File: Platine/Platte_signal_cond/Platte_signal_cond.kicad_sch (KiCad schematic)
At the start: 16 parts

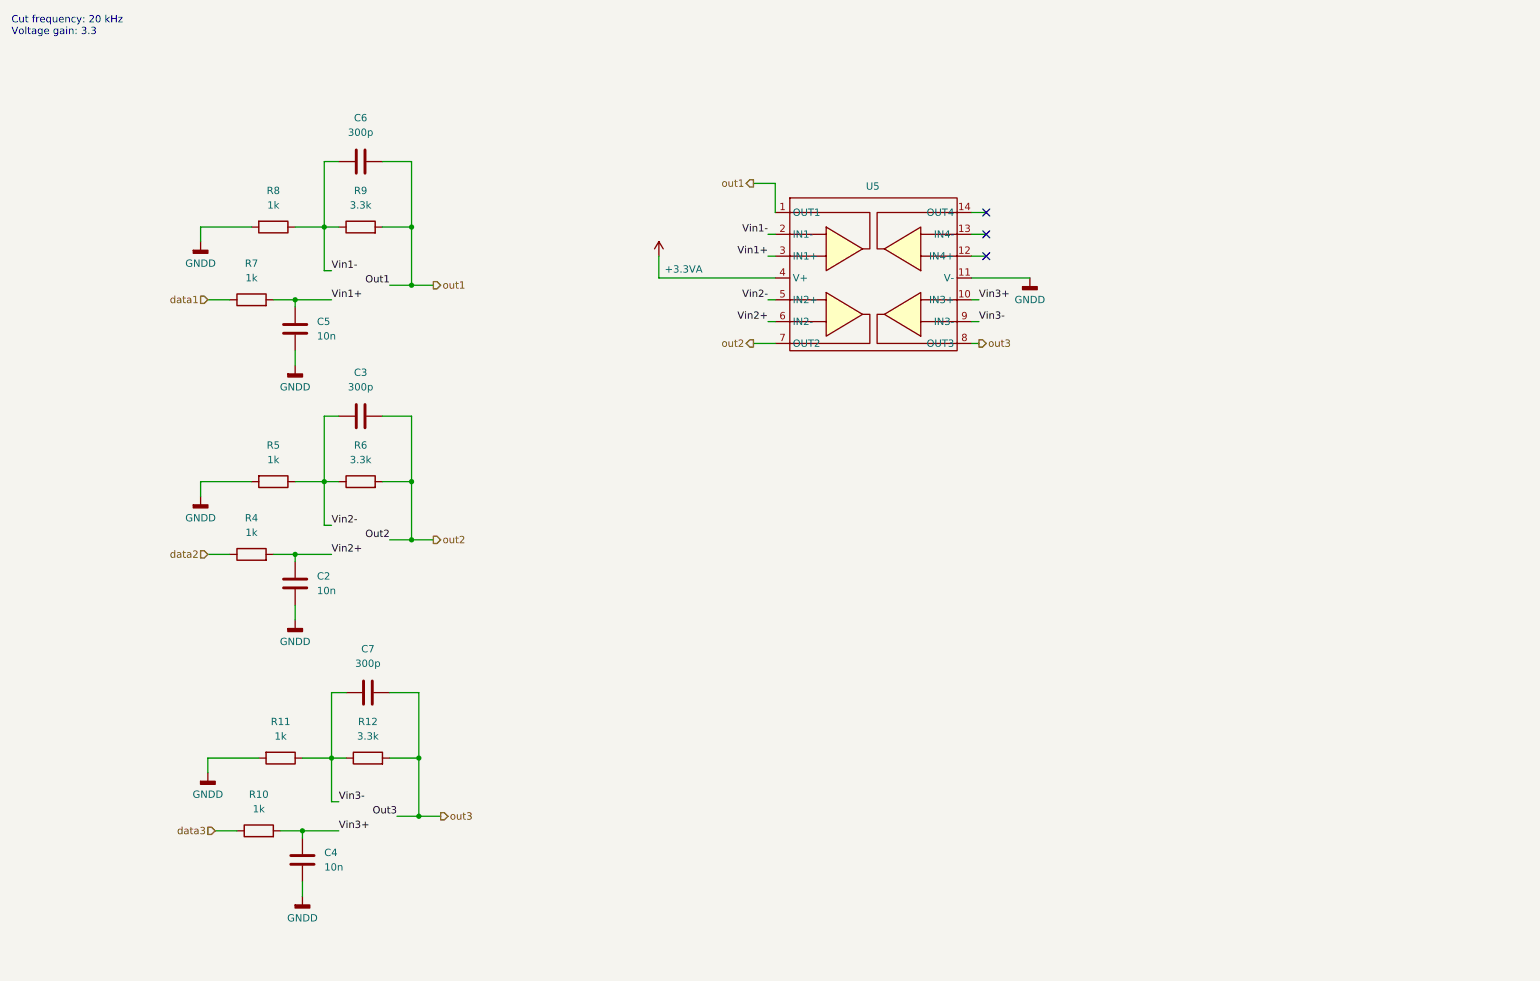
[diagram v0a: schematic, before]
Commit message: Removing CST simulations because of weight, theyre now in the folder outside the repo
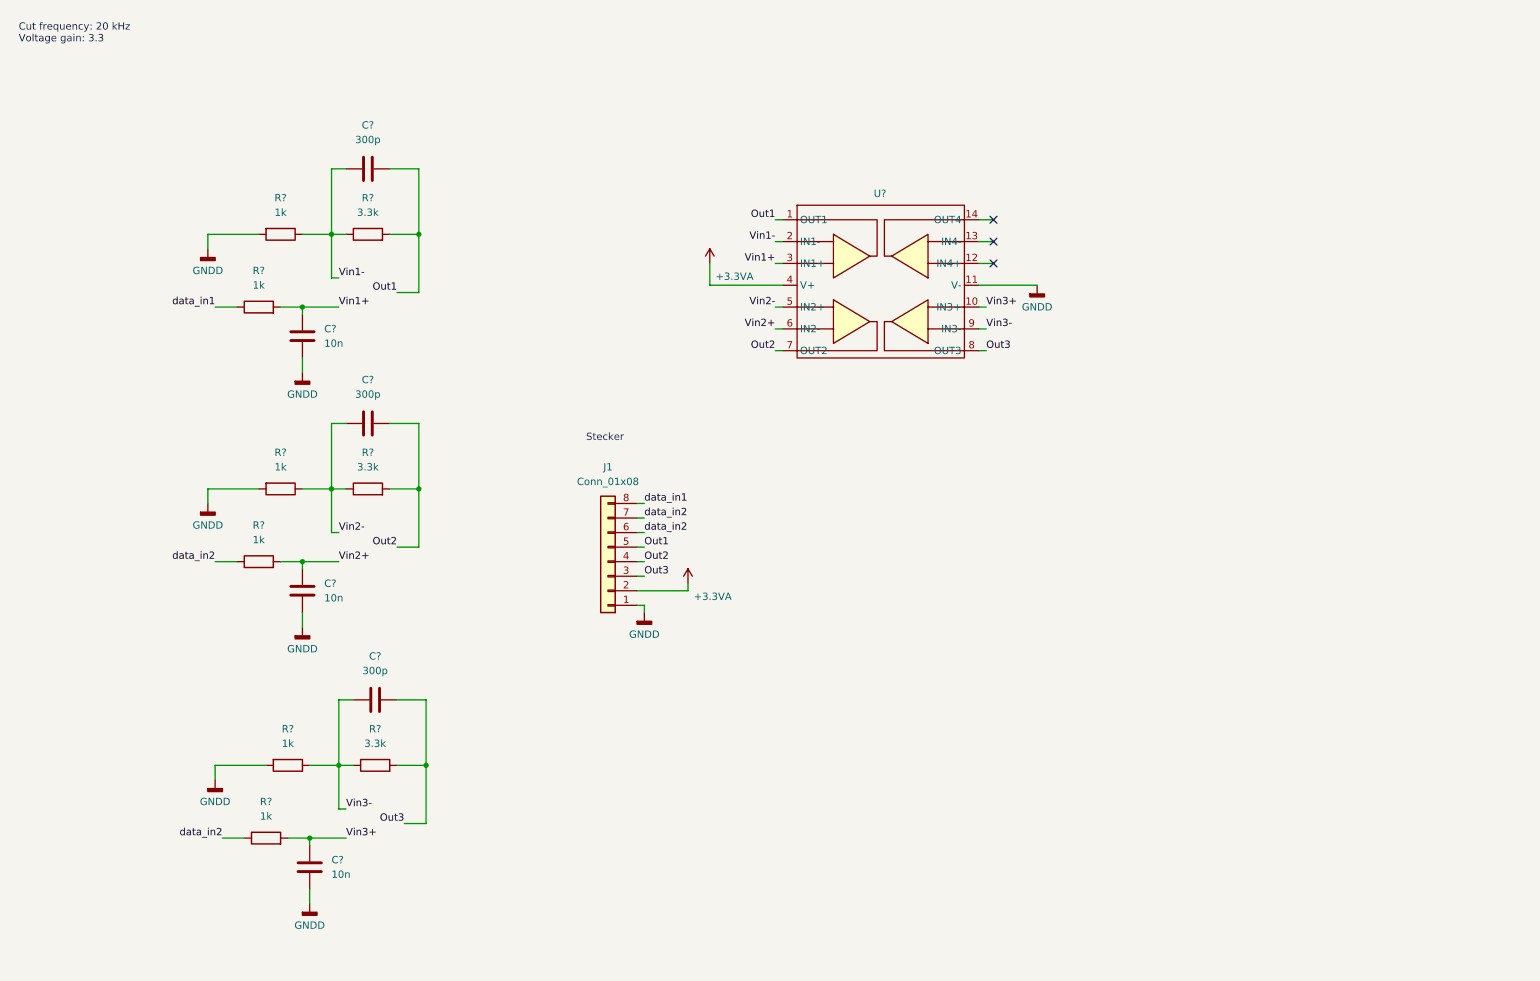
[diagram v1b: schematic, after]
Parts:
- added J1: Conn_01x08, symbol Connector_Generic:Conn_01x08
- U?: renamed from U5; footprint Package_SO:SOIC-14_3.9x8.7mm_P1.27mm -> (none)
- renumbered C4 to C?, C5 to C?, C7 to C?, C3 to C?, C2 to C?, C6 to C?, R4 to R?, R10 to R?, R7 to R?, R11 to R?, R6 to R?, R8 to R?, R12 to R?, R9 to R?, R5 to R?
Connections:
- net data3 is gone; now on net data_in2: R?.1
- net +3.3VA: now also J1.2 (Pin_2)
- net GNDD: now also J1.1 (Pin_1)
- net data1 renamed data_in1
- net data_in1: now also J1.8 (Pin_8)
- net data2 renamed data_in2
- net data_in2: now also J1.6 (Pin_6), J1.7 (Pin_7)
- net out1 renamed Out1
- net Out1: now also J1.5 (Pin_5)
- net out2 renamed Out2
- net Out2: now also J1.4 (Pin_4)
- net out3 renamed Out3
- net Out3: now also J1.3 (Pin_3)
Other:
- note added: "Stecker"
- moved on the sheet: C?, R?, U?

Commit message: Adding footprints to signal conditioning PCB and placing components
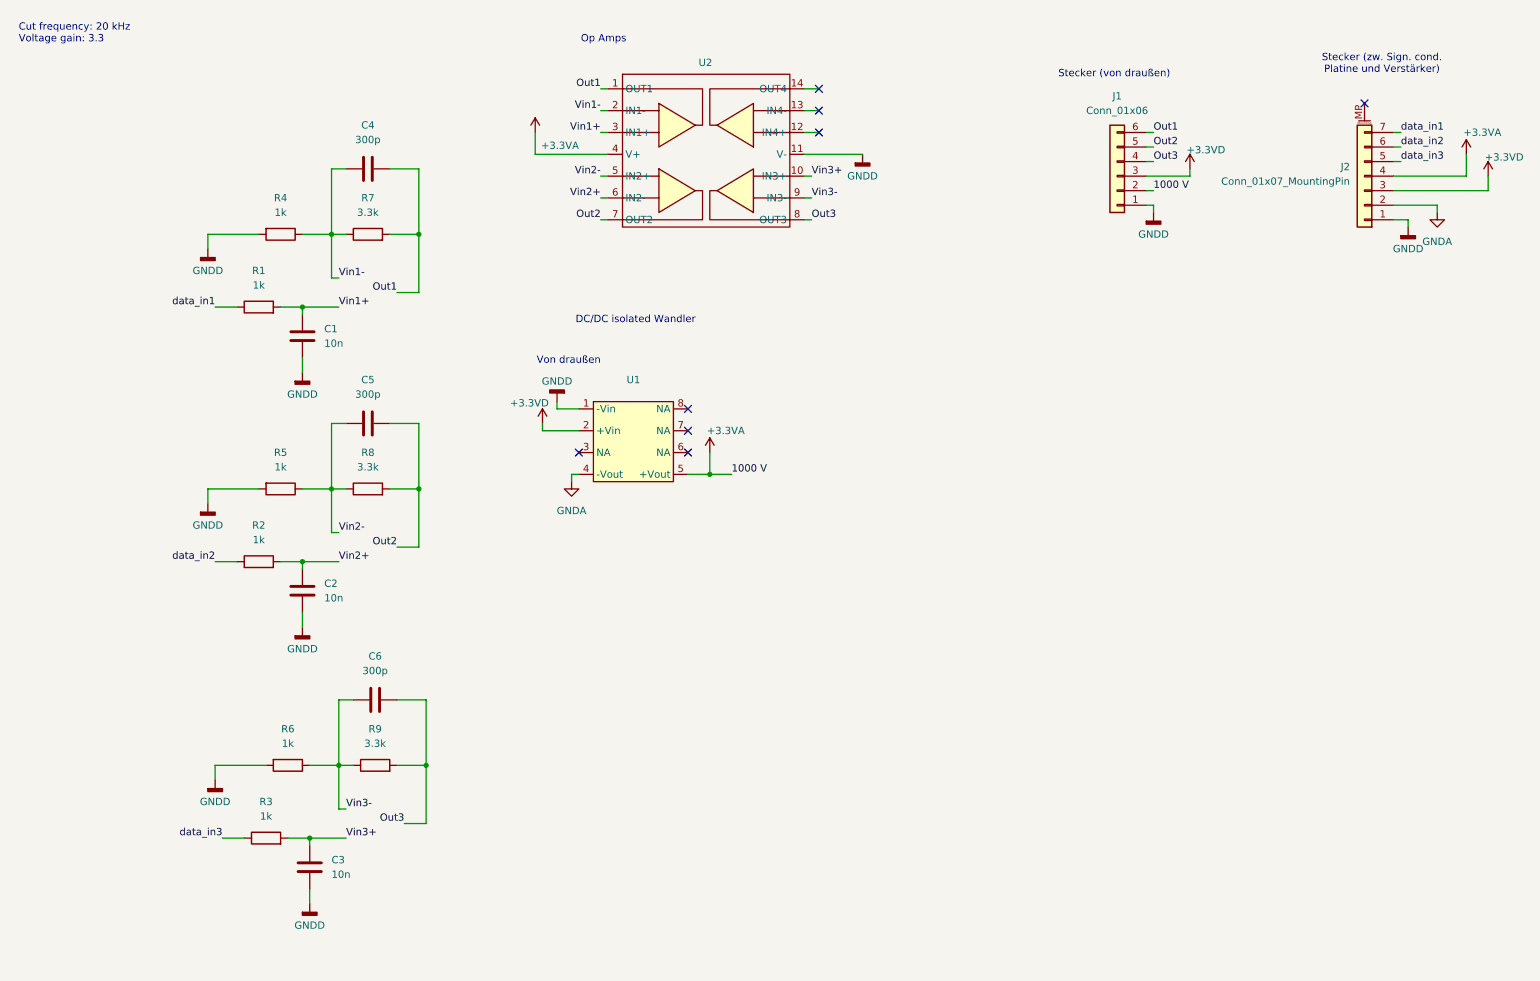
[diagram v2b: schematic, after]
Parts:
- removed J1: Conn_01x08, symbol Connector_Generic:Conn_01x08
- added J1: Conn_01x06, Connector_JST:JST_EH_B6B-EH-A_1x06_P2.50mm_Vertical, symbol Connector_Generic:Conn_01x06
- added J2: Conn_01x07_MountingPin, Connector_JST:JST_GH_BM07B-GHS-TBT_1x07-1MP_P1.25mm_Vertical, symbol Connector_Generic_MountingPin:Conn_01x07_MountingPin
- added U1: ~, Package_DIP:SMDIP-8_W9.53mm, symbol NTE0303MC:NTE0303MC
- U2: renamed from U?; footprint (none) -> Package_SO:SOIC-14_3.9x8.7mm_P1.27mm
- gave numbers to parts that had none: 15
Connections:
- net +3.3VA: now also J1.2 (Pin_2), J2.4 (Pin_4), U1.5 (+Vout)
- net GNDD: now also J1.1 (Pin_1), J2.1 (Pin_1), U1.1 (-Vin)
- net Out1: now also J1.6 (Pin_6)
- net Out2: now also J1.5 (Pin_5)
- net Out3: now also J1.4 (Pin_4)
- net data_in1: now also J2.7 (Pin_7)
- net data_in2: now also J2.6 (Pin_6); no longer R3.1
- new net +3.3VD: J1.3 (Pin_3), J2.3 (Pin_3), U1.2 (+Vin)
- new net GNDA: J2.2 (Pin_2), U1.4 (-Vout)
- new net data_in3: J2.5 (Pin_5), R3.1
- no-connect marks 3 -> 8
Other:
- note added: "DC/DC isolated Wandler"
- note added: "Op Amps"
- note added: "Stecker (von draußen)"
- note added: "Stecker (zw. Sign. cond. Platine und Verstärker)"
- note added: "Von draußen"
- note removed: "Stecker"
- moved on the sheet: U2

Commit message: PCBs almost finished
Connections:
- net +3.3VA: no longer U2.4 (V+)
- net +3.3VD: now also U2.4 (V+)
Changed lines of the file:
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@@
 	(wire
 		(pts
-			(xy 107.95 35.56) (xy 107.95 39.37)
-		)
-		(stroke
-			(width 0)
-			(type default)
-		)
-	)
-	(wire
-		(pts
 			(xy 72.39 41.91) (xy 72.39 53.34)
 		)
@@
 	(wire
 		(pts
-			(xy 73.66 134.62) (xy 73.66 146.05)
+			(xy 111.76 39.37) (xy 111.76 38.1)
 		)
 		(stroke
@@
 	(wire
 		(pts
-			(xy 119.38 35.56) (xy 120.65 35.56)
+			(xy 73.66 134.62) (xy 73.66 146.05)
 		)
 		(stroke
@@
 	(wire
 		(pts
-			(xy 68.58 158.75) (xy 74.93 158.75)
+			(xy 119.38 35.56) (xy 120.65 35.56)
 		)
 		(stroke
@@
 	(wire
 		(pts
-			(xy 63.5 110.49) (xy 67.31 110.49)
+			(xy 68.58 158.75) (xy 74.93 158.75)
 		)
 		(stroke
@@
 	(wire
 		(pts
-			(xy 107.95 39.37) (xy 120.65 39.37)
+			(xy 63.5 110.49) (xy 67.31 110.49)
 		)
 		(stroke
@@
 	(wire
 		(pts
+			(xy 120.65 39.37) (xy 111.76 39.37)
+		)
+		(stroke
+			(width 0)
+			(type default)
+		)
+	)
+	(wire
+		(pts
 			(xy 119.38 27.94) (xy 120.65 27.94)
 		)
@@
 	)
 	(symbol
+		(lib_name "+3.3V_1")
+		(lib_id "power:+3.3V")
+		(at 111.76 38.1 0)
+		(unit 1)
+		(exclude_from_sim no)
+		(in_bom yes)
+		(on_board yes)
+		(dnp no)
+		(property "Reference" "#PWR011"
+			(at 111.76 41.91 0)
+			(effects
+				(font
+					(size 1.27 1.27)
+				)
+				(hide yes)
+			)
+		)
+		(property "Value" "+3.3VD"
+			(at 109.474 34.544 0)
+			(effects
+				(font
+					(size 1.27 1.27)
+				)
+			)
+		)
+		(property "Footprint" ""
+			(at 111.76 38.1 0)
+			(effects
+				(font
+					(size 1.27 1.27)
+				)
+				(hide yes)
+			)
+		)
+		(property "Datasheet" ""
+			(at 111.76 38.1 0)
+			(effects
+				(font
+					(size 1.27 1.27)
+				)
+				(hide yes)
+			)
+		)
+		(property "Description" "Power symbol creates a global label with name \"+3.3V\""
+			(at 111.76 38.1 0)
+			(effects
+				(font
+					(size 1.27 1.27)
+				)
+				(hide yes)
+			)
+		)
+		(pin "1"
+		)
+		(instances
+			(project "Platte_signal_cond"
+				(path "/40ada750-8e3f-4b83-a748-c38cd6a4aff7"
+					(reference "#PWR011")
+					(unit 1)
+				)
+			)
+		)
+	)
+	(symbol
 		(lib_id "power:+3.3V")
 		(at 270.51 39.37 0)
@@
 					(unit 1)
 				)
-			)
-		)
-	)
-	(symbol
-		(lib_id "power:+3.3V")
-		(at 107.95 35.56 0)
-		(unit 1)
-		(exclude_from_sim no)
-		(in_bom yes)
-		(on_board yes)
-		(dnp no)
-		(property "Reference" "#PWR0107"
-			(at 107.95 39.37 0)
-			(effects
-				(font
-					(size 1.27 1.27)
-				)
-				(hide yes)
-			)
-		)
-		(property "Value" "+3.3VA"
-			(at 108.966 37.846 0)
-			(effects
-				(font
-					(size 1.27 1.27)
-				)
-				(justify left)
-			)
-		)
-		(property "Footprint" ""
-			(at 107.95 35.56 0)
-			(effects
-				(font
-					(size 1.27 1.27)
-				)
-				(hide yes)
-			)
-		)
-		(property "Datasheet" ""
-			(at 107.95 35.56 0)
-			(effects
-				(font
-					(size 1.27 1.27)
-				)
-				(hide yes)
-			)
-		)
-		(property "Description" ""
-			(at 107.95 35.56 0)
-			(effects
-				(font
-					(size 1.27 1.27)
-				)
-				(hide yes)
-			)
-		)
-		(pin "1"
-		)
-		(instances
-			(project "Platte_signal_cond"
-				(path "/40ada750-8e3f-4b83-a748-c38cd6a4aff7"
-					(reference "#PWR0107")
-					(unit 1)
-				)
-			)
-			(project "Platte"
-				(path "/8ec2d373-240e-44f6-ab9e-7e8ab23831f1/b3951852-0f57-416d-a61f-79016a17622d"
-					(reference "#PWR02")
-					(unit 1)
-				)

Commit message: Mit Robin geredet, ein paar Veränderung gemacht
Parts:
- added R10: 3.3k, Resistor_SMD:R_0201_0603Metric_Pad0.64x0.40mm_HandSolder, symbol Device:R
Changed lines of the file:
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@@
+	)
+	(symbol
+		(lib_id "Device:R")
+		(at 96.52 68.58 180)
+		(unit 1)
+		(exclude_from_sim no)
+		(in_bom yes)
+		(on_board yes)
+		(dnp no)
+		(fields_autoplaced yes)
+		(property "Reference" "R10"
+			(at 99.06 67.3099 0)
+			(effects
+				(font
+					(size 1.27 1.27)
+				)
+				(justify right)
+			)
+		)
+		(property "Value" "3.3k"
+			(at 99.06 69.8499 0)
+			(effects
+				(font
+					(size 1.27 1.27)
+				)
+				(justify right)
+			)
+		)
+		(property "Footprint" "Resistor_SMD:R_0201_0603Metric_Pad0.64x0.40mm_HandSolder"
+			(at 98.298 68.58 90)
+			(effects
+				(font
+					(size 1.27 1.27)
+				)
+				(hide yes)
+			)
+		)
+		(property "Datasheet" "~"
+			(at 96.52 68.58 0)
+			(effects
+				(font
+					(size 1.27 1.27)
+				)
+				(hide yes)
+			)
+		)
+		(property "Description" "Resistor"
+			(at 96.52 68.58 0)
+			(effects
+				(font
+					(size 1.27 1.27)
+				)
+				(hide yes)
+			)
+		)
+		(pin "1"
+		)
+		(pin "2"
+		)
+		(instances
+			(project "Platte_signal_cond"
+				(path "/40ada750-8e3f-4b83-a748-c38cd6a4aff7"
+					(reference "R10")
+					(unit 1)
+				)
+			)
+		)
 	)
 	(symbol

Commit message: PCBs ready
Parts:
- removed C1, C2, C3: 10n, Capacitor_SMD:C_0201_0603Metric_Pad0.64x0.40mm_HandSolder, symbol Device:C
- removed R1, R2, R3: 1k, Resistor_SMD:R_0201_0603Metric_Pad0.64x0.40mm_HandSolder, symbol Device:R
- removed R10: 3.3k, Resistor_SMD:R_0201_0603Metric_Pad0.64x0.40mm_HandSolder, symbol Device:R
- C4, C5, C6: value 300p -> 1.85n; footprint Capacitor_SMD:C_0201_0603Metric_Pad0.64x0.40mm_HandSolder -> Capacitor_SMD:C_0603_1608Metric_Pad1.08x0.95mm_HandSolder
- R4, R5, R6: footprint Resistor_SMD:R_0201_0603Metric_Pad0.64x0.40mm_HandSolder -> Resistor_SMD:R_0603_1608Metric_Pad0.98x0.95mm_HandSolder
- R7, R8, R9: value 3.3k -> 270; footprint Resistor_SMD:R_0201_0603Metric_Pad0.64x0.40mm_HandSolder -> Resistor_SMD:R_0603_1608Metric_Pad0.98x0.95mm_HandSolder
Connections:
- net data_in1 is gone; now on net Vin2+: J2.7 (Pin_7)
- net data_in2 is gone; now on net Vin1+: J2.6 (Pin_6)
- net data_in3 is gone; now on net Vin3+: J2.5 (Pin_5)

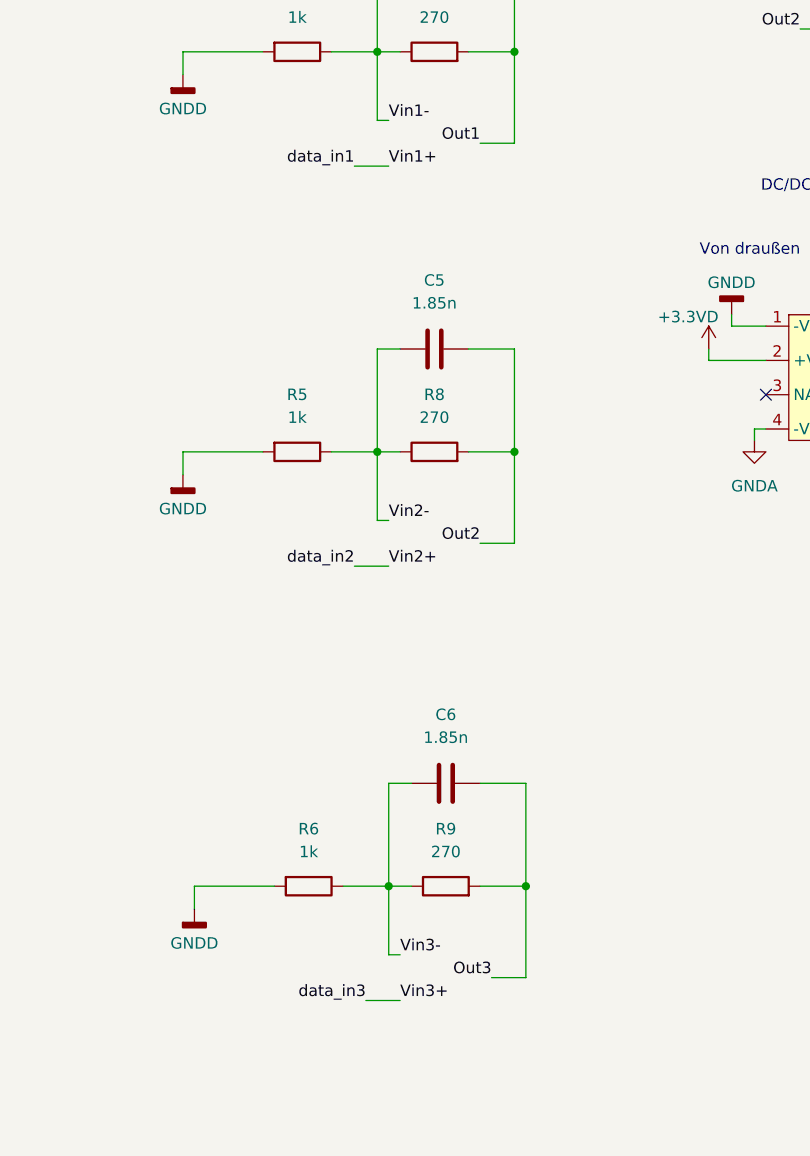
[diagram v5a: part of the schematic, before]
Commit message: Modifying working frequency in LTSpice and adding extra resistor in pcb
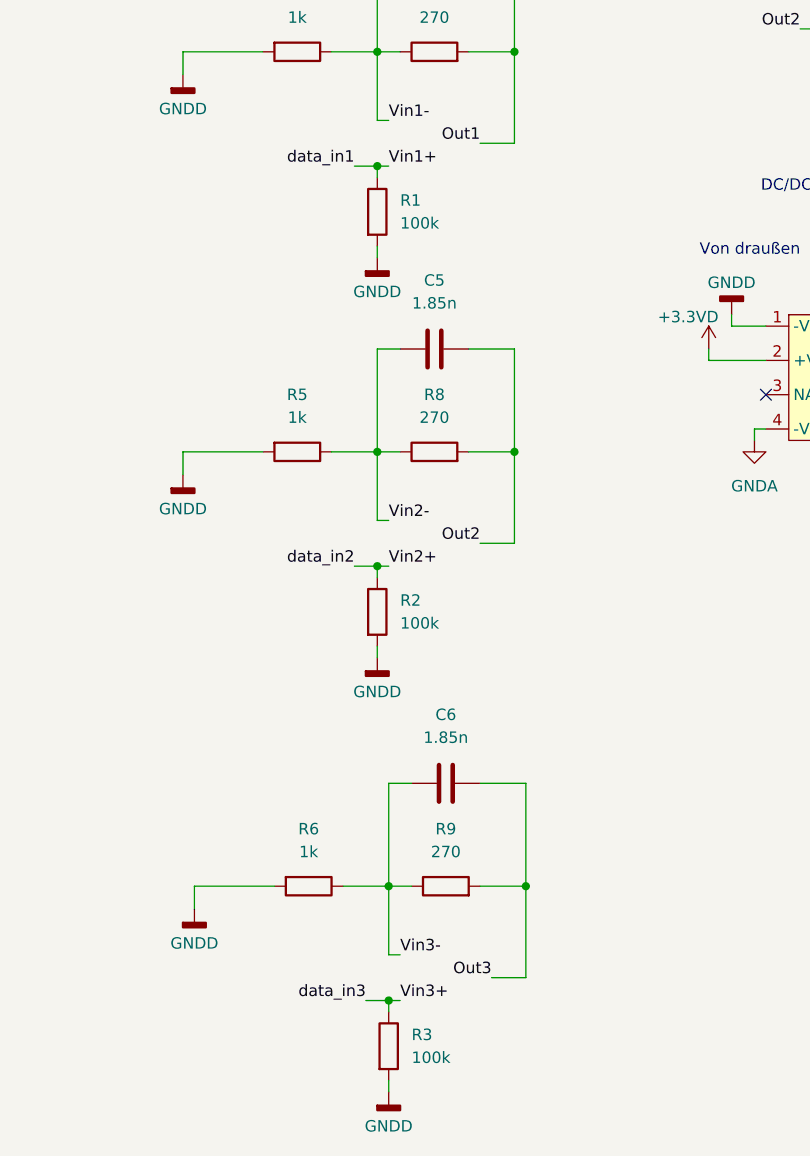
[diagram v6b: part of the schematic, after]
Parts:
- added R1, R2, R3: 100k, Resistor_SMD:R_0603_1608Metric_Pad0.98x0.95mm_HandSolder, symbol Device:R
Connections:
- net GNDD: now also R1.2, R2.2, R3.2
- net Vin1+: now also R1.1
- net Vin2+: now also R2.1
- net Vin3+: now also R3.1
